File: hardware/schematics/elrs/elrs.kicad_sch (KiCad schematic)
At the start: 34 parts, among them U13 ESP32-C3FH4, U14 TLV75533PDQNR, U15 SX1281IMLTRT, X2 CJ17-400001010B20

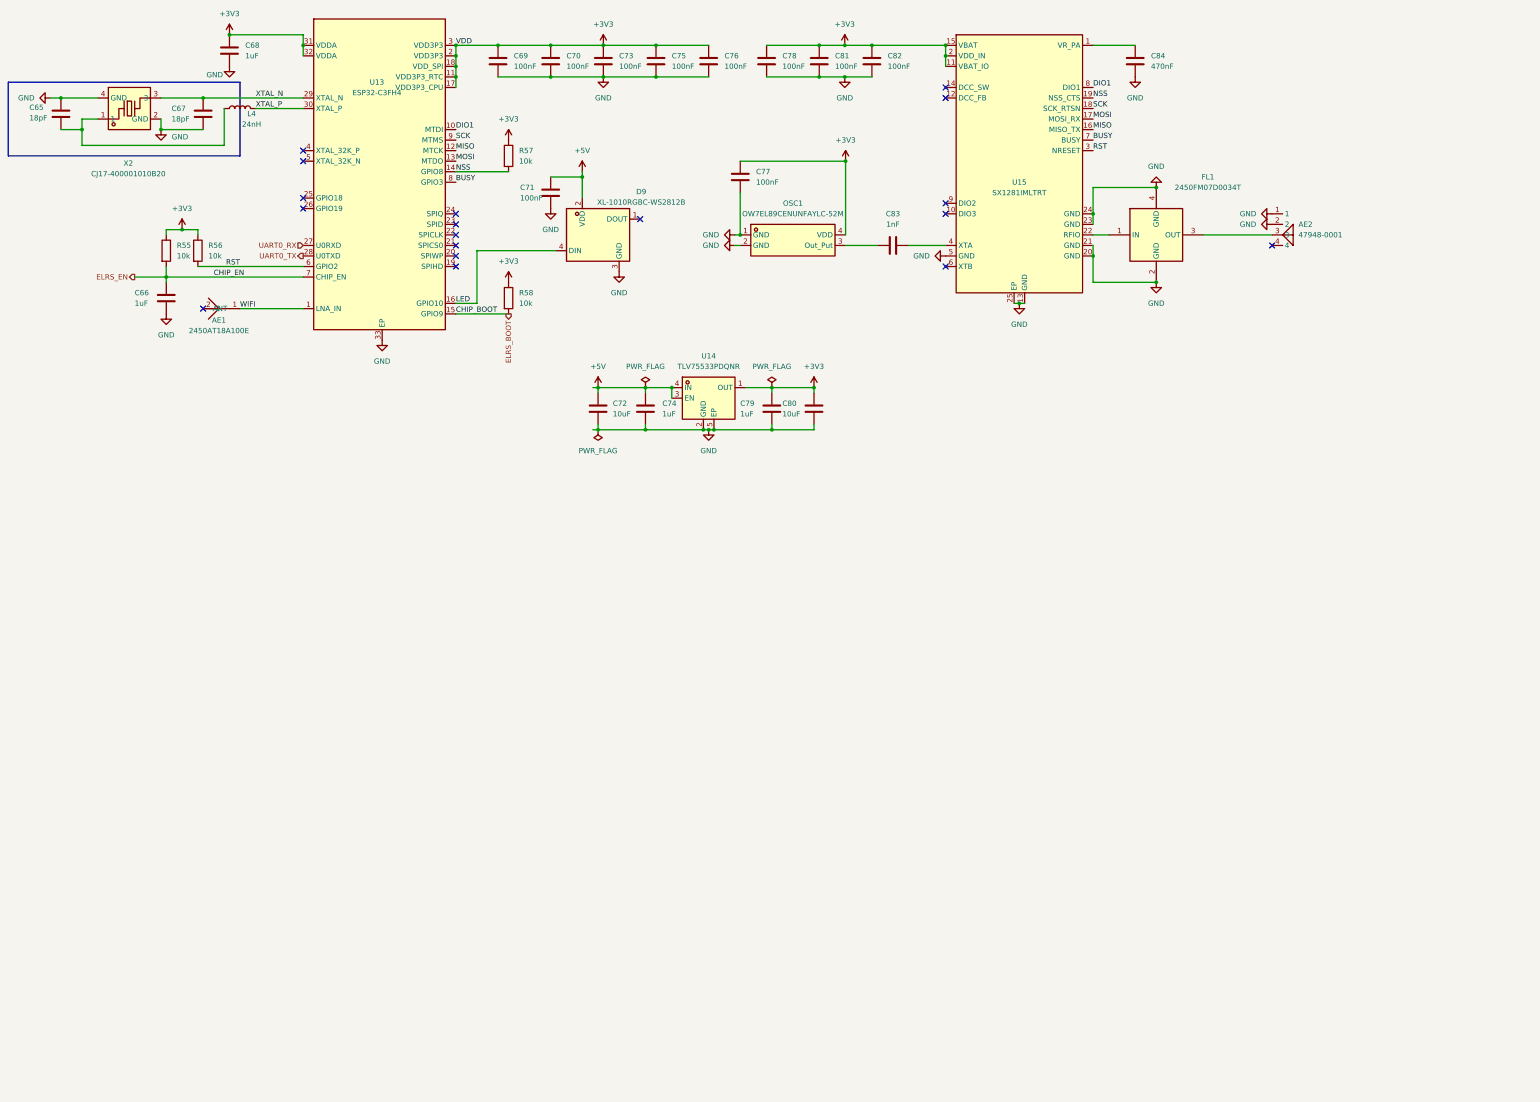
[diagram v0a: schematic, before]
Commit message: Refresh design sources: import rev2 sheets + libs from current sibling repos
FC sheets   <- OpenFC-Lite-Mini rev2 (RP2354A, LMR51430 power tree, COS8051 OSD)
ESC sheets  <- 4in1-mini Rev2 (AT32F421 + NSG2065Q + DOY180N03T, INA186 CSA)
ELRS sheet  <- OpenRX-Lite (ESP32-C3 + SX1281, chip antenna)

Drop-in swaps at paths the root sheet already references; esc_channel
instantiated 4x from root resolves. esc_main.kicad_sch (4in1-mini top:
buck/LDO/CSA/TVS/connector) kept as reference, with ESC.kicad_sch beside
it so its internal channel instances resolve if ever instantiated.

Libraries replaced wholesale: lib(.kicad_sym/.pretty/.3dshapes) from
OpenFC-Lite-Mini, components+4in1ESC from 4in1-mini, OpenRX-Shared from
OpenRX. 3D model paths in OpenRX-Shared.pretty rewritten to project-
local via pcbnew API. Hierarchy verified with kicad-cli netlist export.

Supersedes the 2026-04 port from OpenFC-ECO V0.3 / 4in1ESC 2 (in git
history). Schematic re-annotation + root rewiring is manual work in
KiCad. Old PCB layout retained; footprints are embedded so it opens,
but layout predates this refresh.

Co-Authored-By: Claude Fable 5 <noreply@anthropic.com>
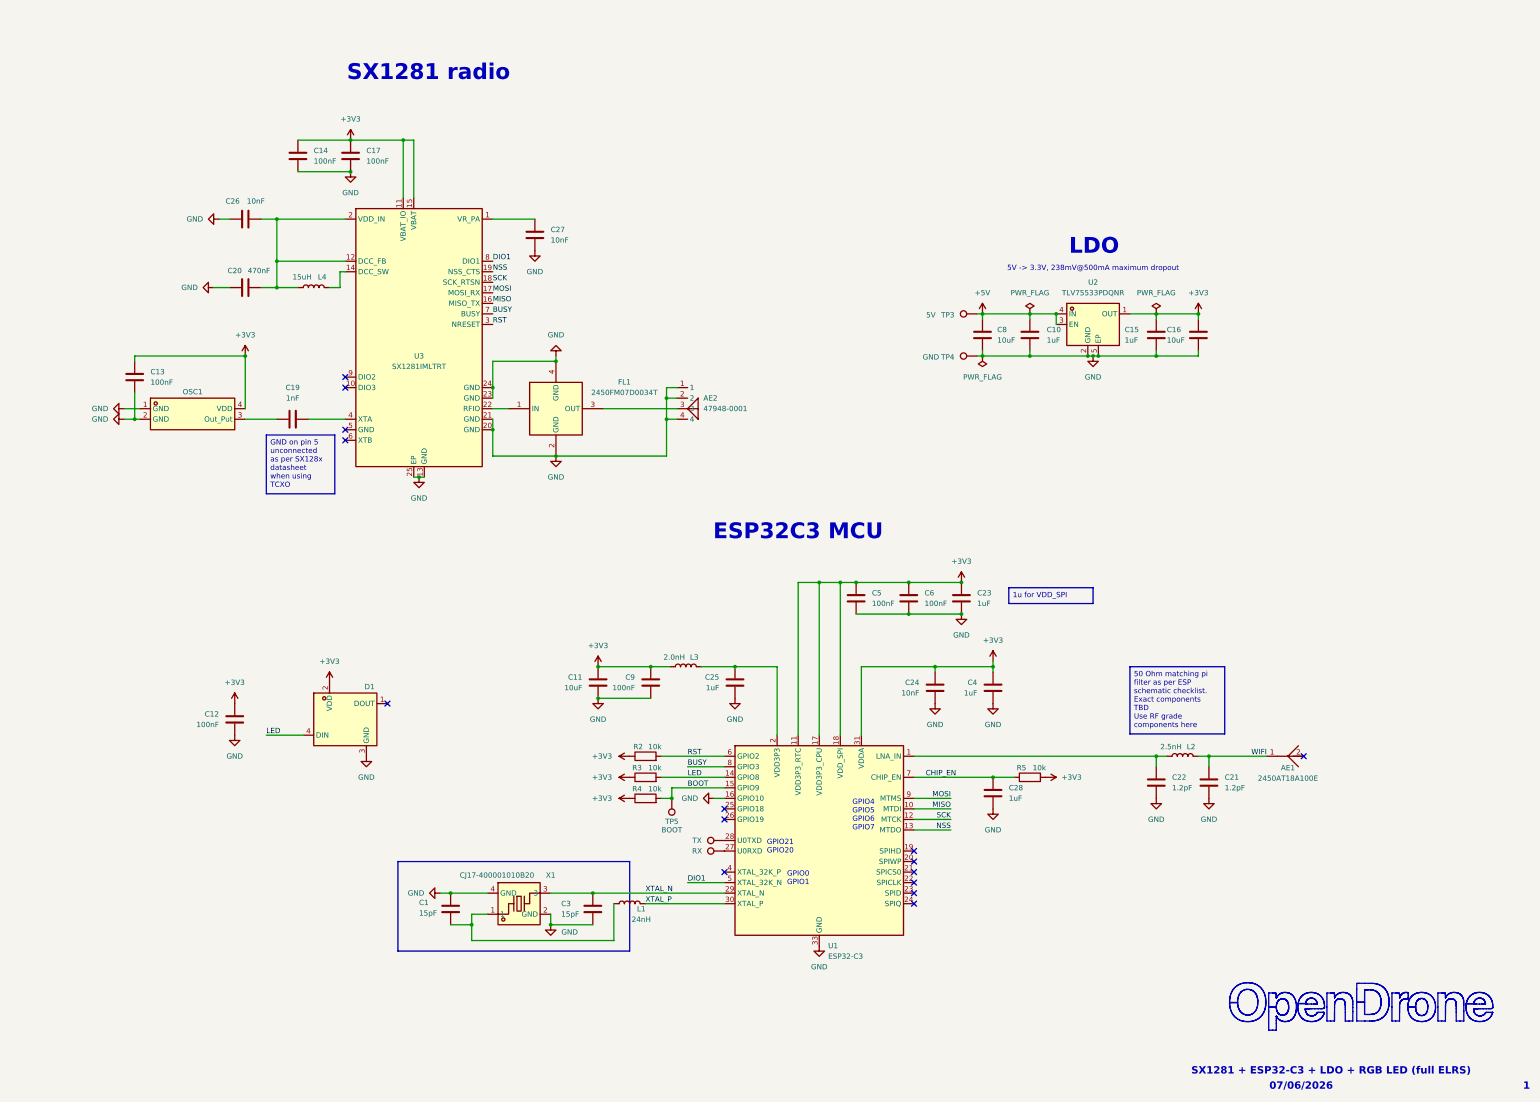
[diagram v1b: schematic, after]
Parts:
- removed AE1: 2450AT18A100E, lib:ANT-SMD_L3.2-W1.6, symbol lib:2450AT18A100E
- removed AE2: 47948-0001, lib:ANT-SMD_47948-0001, symbol lib:47948-0001
- removed C65, C67: 18pF, Capacitor_SMD:C_0201_0603Metric, symbol Device:C
- removed C66, C68: 1uF, Capacitor_SMD:C_0201_0603Metric, symbol Device:C
- removed C69, C70, C71, C73, C75, C76, C78, C81, C82: 100nF, Capacitor_SMD:C_0201_0603Metric, symbol Device:C
- removed C84: 470nF, Capacitor_SMD:C_0201_0603Metric, symbol Device:C
- removed D9: XL-1010RGBC-WS2812B, lib:LED-SMD_4P-L1.0-W1.0-TL_XL-1010RGBC-WS2812B, symbol lib:XL-1010RGBC-WS2812B
- removed FL1: 2450FM07D0034T, lib:FILTER-SMD_4P-L1.0-W0.5-L, symbol lib:2450FM07D0034T
- removed R55, R56, R57, R58: 10k, Resistor_SMD:R_0201_0603Metric, symbol Device:R
- removed U13: ESP32-C3FH4, lib:QFN-32_L5.0-W5.0-P0.50-TL-EP3.7, symbol lib:ESP32-C3FH4
- removed X2: CJ17-400001010B20, lib:CRYSTAL-SMD_4P-L1.6-W1.2-BL, symbol lib:CJ17-400001010B20
- added AE1: 2450AT18A100E, OpenRX-Shared:ANT-SMD_L3.2-W1.6, symbol OpenRX-Shared:2450AT18A100E
- added AE2: 47948-0001, OpenRX-Shared:ANT-SMD_47948-0001, symbol OpenRX-Shared:47948-0001
- added C1, C3: 15pF, Capacitor_SMD:C_0201_0603Metric, symbol Device:C
- added C11: 10uF, Capacitor_SMD:C_0402_1005Metric, symbol Device:C
- added C12, C14, C17, C5, C6, C9: 100nF, Capacitor_SMD:C_0201_0603Metric, symbol Device:C
- added C20: 470nF, Capacitor_SMD:C_0201_0603Metric, symbol Device:C
- added C21, C22: 1.2pF, Capacitor_SMD:C_0201_0603Metric, symbol Device:C
- added C23, C25, C28, C4: 1uF, Capacitor_SMD:C_0201_0603Metric, symbol Device:C
- added C24, C26, C27: 10nF, Capacitor_SMD:C_0201_0603Metric, symbol Device:C
- added D1: XL-1010RGBC-WS2812B, OpenRX-Shared:LED-SMD_4P-L1.0-W1.0-TL_XL-1010RGBC-WS2812B, symbol OpenRX-Shared:XL-1010RGBC-WS2812B
- added FL1: 2450FM07D0034T, OpenRX-Shared:FILTER-SMD_4P-L1.0-W0.5-L, symbol OpenRX-Shared:2450FM07D0034T
- added L1: 24nH, Inductor_SMD:L_0201_0603Metric, symbol Device:L
- added L2: 2.5nH, Inductor_SMD:L_0201_0603Metric, symbol Device:L
- added L3: 2.0nH, Inductor_SMD:L_0201_0603Metric, symbol Device:L
- added R2, R3, R4, R5: 10k, Resistor_SMD:R_0201_0603Metric, symbol Device:R
- added TP1: RX, OpenRX-Shared:SolderPad_1.2x2.0mm, symbol Connector:TestPoint
- added TP2: TX, OpenRX-Shared:SolderPad_1.2x2.0mm, symbol Connector:TestPoint
- added TP3: 5V, OpenRX-Shared:SolderPad_1.2x2.0mm, symbol Connector:TestPoint
- added TP4: GND, OpenRX-Shared:SolderPad_1.2x2.0mm, symbol Connector:TestPoint
- added TP5: BOOT, OpenRX-Shared:SolderPad_1.2x2.0mm, symbol Connector:TestPoint
- added U1: ESP32-C3, Package_DFN_QFN:QFN-32-1EP_5x5mm_P0.5mm_EP3.7x3.7mm, symbol MCU_Espressif:ESP32-C3
- added X1: CJ17-400001010B20, OpenRX-Shared:CRYSTAL-SMD_4P-L1.6-W1.2-BL, symbol OpenRX-Shared:CJ17-400001010B20
- C10: renamed from C74; LCSC Part (none) -> C76935
- C13: renamed from C77; LCSC Part (none) -> C76939
- C15: renamed from C79; LCSC Part (none) -> C76935
- C16: renamed from C80; LCSC Part (none) -> C15525
- C19: renamed from C83; LCSC Part (none) -> C66942
- C8: renamed from C72; LCSC Part (none) -> C15525
- L4: value 24nH -> 15uH; footprint Inductor_SMD:L_0201_0603Metric -> Inductor_SMD:L_0805_2012Metric; LCSC C206441 -> (none)
- OSC1: footprint lib:OSC-SMD_4P-L2.0-W1.6-BL_TXC_7Z -> OpenRX-Shared:OSC-SMD_4P-L2.0-W1.6-BL_TXC_7Z; symbol lib:OW7EL89CENUNFAYLC-52M -> OpenRX-Shared:OW7EL89CENUNFAYLC-52M
- U2: renamed from U14; footprint lib:X2SON-4_L1.0-W1.0-P0.65-TL-EP -> OpenRX-Shared:X2SON-4_L1.0-W1.0-P0.65-TL-EP; symbol lib:TLV75533PDQNR -> OpenRX-Shared:TLV75533PDQNR
- U3: renamed from U15; footprint lib:QFN-24_L4.0-W4.0-P0.50-TL-EP2.6 -> OpenRX-Shared:QFN-24_L4.0-W4.0-P0.50-TL-EP2.6; symbol lib:SX1281IMLTRT -> OpenRX-Shared:SX1281IMLTRT
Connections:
- net +3V3: now also C11.1, C12.1, C14.1, C17.1, C23.1, C24.1, C4.1, C5.1, C6.1, C9.1, D1.2 (VDD), L3.2, R2.1, R3.1, R4.1, R5.2, U1.11 (VDD3P3_RTC), U1.17 (VDD3P3_CPU), U1.18 (VDD_SPI), U1.31 (VDDA), U1.32 (VDDA); no longer U3.2 (VDD_IN)
- net +5V: now also TP3.1
- net BUSY: now also U1.8 (GPIO3)
- net DIO1: now also U1.5 (XTAL_32K_N)
- net GND: now also AE2.1, AE2.2, AE2.4, C1.2, C11.2, C12.2, C14.2, C17.2, C20.1, C21.2, C22.2, C23.2, C24.2, C25.2, C26.1, C27.2, C28.2, C3.2, C4.2, C5.2, C6.2, C9.2, D1.3 (GND), FL1.2 (GND), FL1.4 (GND), TP4.1, U1.16 (GPIO10), U1.33 (GND), X1.2 (GND), X1.4 (GND); no longer U3.5 (GND)
- net LED: now also D1.4 (DIN), R3.2, U1.14 (GPIO8)
- net MISO: now also U1.10 (MTDI)
- net MOSI: now also U1.9 (MTMS)
- net NSS: now also U1.13 (MTDO)
- net RST: now also R2.2, U1.6 (GPIO2)
- net SCK: now also U1.12 (MTCK)
- net WIFI: now also AE1.1, C21.1, L2.1
- net XTAL_N: now also C3.1, U1.29 (XTAL_N), X1.3
- net XTAL_P: now also L1.2, U1.30 (XTAL_P); no longer L4.2
- net at L4.1: now also U3.12 (DCC_FB), U3.2 (VDD_IN), C20.2, C26.2
- net at U3.22 (RFIO): now also FL1.1 (IN)
- net at U3.1 (VR_PA): now also C27.1
- net at U3.14 (DCC_SW): now also L4.2
- new net: C1.1, L1.1, X1.1
- new net: C25.1, L3.1, U1.2 (VDD3P3), U1.3 (VDD3P3)
- new net: AE2.3, FL1.3 (OUT)
- new net: C22.1, L2.2, U1.1 (LNA_IN)
- new net: TP1.1, U1.27 (U0RXD)
- new net: TP2.1, U1.28 (U0TXD)
- new net BOOT: R4.2, TP5.1, U1.15 (GPIO9)
- new net CHIP_EN: C28.1, R5.1, U1.7 (CHIP_EN)
- no-connect marks 18 -> 15
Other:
- note added: "07/06/2026"
- note added: "1"
- note added: "5V -> 3.3V, 238mV@500mA maximum dropout"
- note added: "ESP32C3 MCU"
- note added: "GPIO0 GPIO1"
- note added: "GPIO21 GPIO20"
- note added: "GPIO4 GPIO5 GPIO6 GPIO7"
- note added: "LDO"
- note added: "SX1281 + ESP32-C3 + LDO + RGB LED (full ELRS)"
- note added: "SX1281 radio"
- moved on the sheet: C10, C13, C15, C16, C19, C8, OSC1, U2, U3
